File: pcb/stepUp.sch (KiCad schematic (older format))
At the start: 14 parts

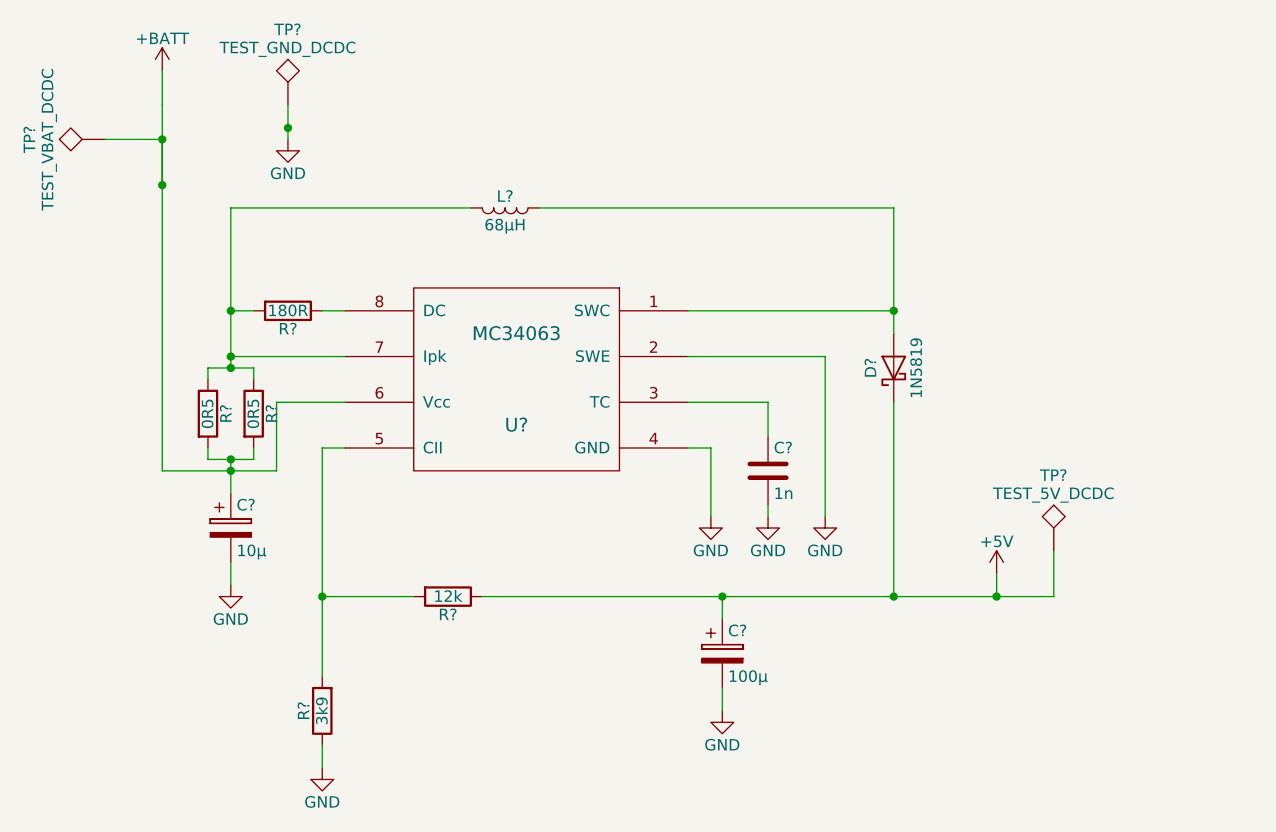
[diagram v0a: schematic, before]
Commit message: nightly | pcb build, routing, placing
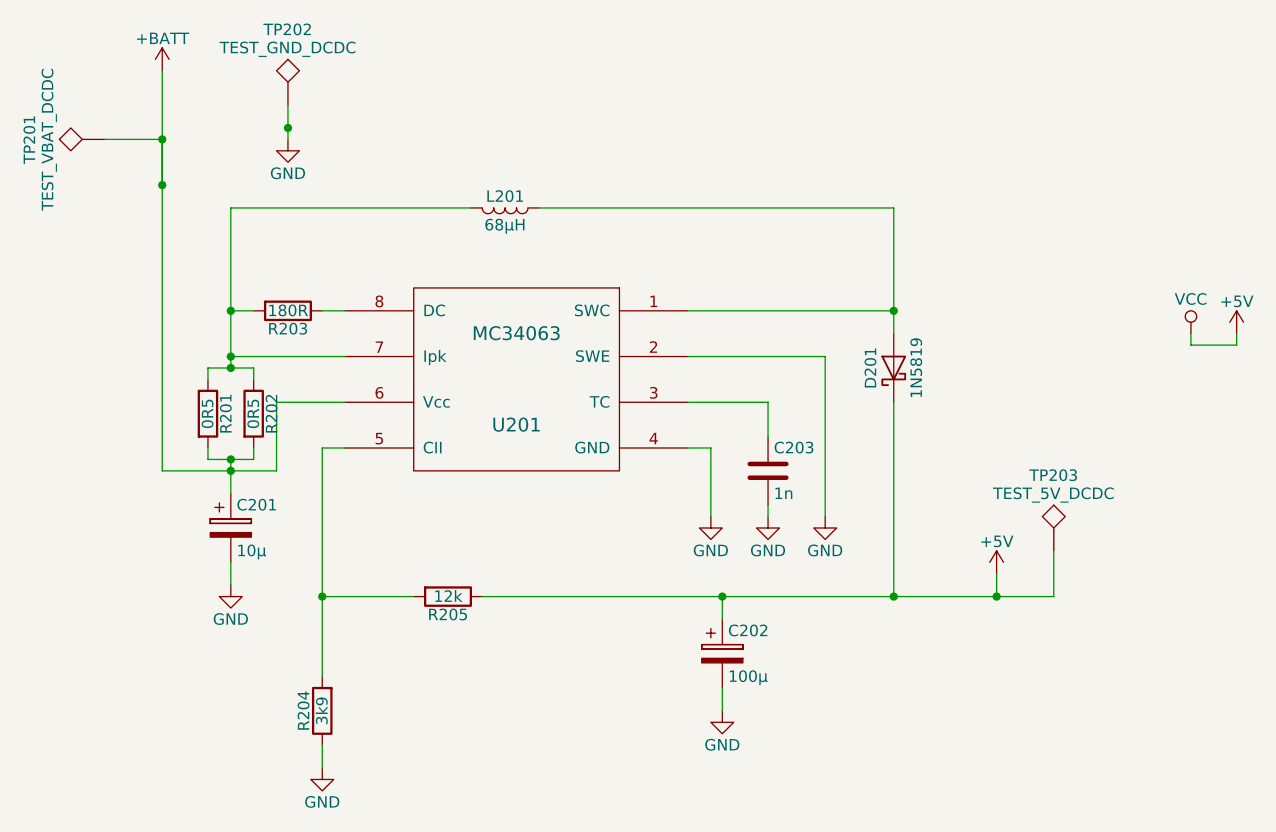
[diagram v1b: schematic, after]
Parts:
- C201, C202: renamed from C?; footprint (none) -> Capacitors_SMD:CP_Elec_10x10.5
- C203: renamed from C?; footprint (none) -> Capacitors_SMD:C_0603_HandSoldering
- D201: renamed from D?; footprint (none) -> Diodes_SMD:D_SMC-RM10_Universal_Handsoldering
- L201: renamed from L?; footprint (none) -> Inductors_SMD:L_Taiyo-Yuden_NR-50xx_HandSoldering
- R201, R202, R203, R204, R205: renamed from R?; footprint (none) -> Resistors_SMD:R_0603_HandSoldering
- TP201, TP202, TP203: renamed from TP?; footprint (none) -> Measurement_Points:Measurement_Point_Round-SMD-Pad_Big
- U201: renamed from U?; footprint (none) -> Housings_SOIC:SOIC-8_3.9x4.9mm_Pitch1.27mm
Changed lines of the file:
@@
 LIBS:contrib
 LIBS:valves
-LIBS:MC34063
 LIBS:adxl345
+LIBS:ws2812b
 LIBS:fantimote-cache
 EELAYER 25 0
@@
 $Descr A4 11693 8268
 encoding utf-8
-Sheet 2 7
+Sheet 2 10
 Title "seniorsRemote (fantimote)"
 Date "2018-07-07"
@@
 $EndDescr
 $Comp
-L MC34063 U?
+L MC34063 U201
 U 1 1 5B367841
 P 2850 2200
-F 0 "U?" H 2850 2000 60  0000 C CNN
+F 0 "U201" H 2850 2000 60  0000 C CNN
 F 1 "MC34063" H 2850 2400 60  0000 C CNN
-F 2 "" H 2850 2200 60  0001 C CNN
+F 2 "Housings_SOIC:SOIC-8_3.9x4.9mm_Pitch1.27mm" H 2850 2200 60  0001 C CNN
 F 3 "" H 2850 2200 60  0001 C CNN
 	1    2850 2200
@@
 $EndComp
 $Comp
-L D_Schottky D?
+L D_Schottky D201
 U 1 1 5B36789E
 P 4500 2150
-F 0 "D?" H 4500 2250 50  0000 C CNN
+F 0 "D201" H 4500 2250 50  0000 C CNN
 F 1 "1N5819" H 4500 2050 50  0000 C CNN
-F 2 "" H 4500 2150 50  0001 C CNN
+F 2 "Diodes_SMD:D_SMC-RM10_Universal_Handsoldering" H 4500 2150 50  0001 C CNN
 F 3 "" H 4500 2150 50  0001 C CNN
 	1    4500 2150
@@
 $EndComp
 $Comp
-L R R?
+L R R204
 U 1 1 5B3678EB
 P 2000 3650
-F 0 "R?" V 2080 3650 50  0000 C CNN
+F 0 "R204" V 2080 3650 50  0000 C CNN
 F 1 "3k9" V 2000 3650 50  0000 C CNN
-F 2 "" V 1930 3650 50  0001 C CNN
+F 2 "Resistors_SMD:R_0603_HandSoldering" V 1930 3650 50  0001 C CNN
 F 3 "" H 2000 3650 50  0001 C CNN
 	1    2000 3650
@@
 $EndComp
 $Comp
-L R R?
+L R R205
 U 1 1 5B367974
 P 2550 3150
-F 0 "R?" V 2630 3150 50  0000 C CNN
+F 0 "R205" V 2630 3150 50  0000 C CNN
 F 1 "12k" V 2550 3150 50  0000 C CNN
-F 2 "" V 2480 3150 50  0001 C CNN
+F 2 "Resistors_SMD:R_0603_HandSoldering" V 2480 3150 50  0001 C CNN
 F 3 "" H 2550 3150 50  0001 C CNN
 	1    2550 3150
@@
 $EndComp
 $Comp
-L R R?
+L R R203
 U 1 1 5B3679D4
 P 1850 1900
-F 0 "R?" V 1930 1900 50  0000 C CNN
+F 0 "R203" V 1930 1900 50  0000 C CNN
 F 1 "180R" V 1850 1900 50  0000 C CNN
-F 2 "" V 1780 1900 50  0001 C CNN
+F 2 "Resistors_SMD:R_0603_HandSoldering" V 1780 1900 50  0001 C CNN
 F 3 "" H 1850 1900 50  0001 C CNN
 	1    1850 1900
@@
 $EndComp
 $Comp
-L CP C?
+L CP C201
 U 1 1 5B367A61
 P 1600 2850
-F 0 "C?" H 1625 2950 50  0000 L CNN
+F 0 "C201" H 1625 2950 50  0000 L CNN
 F 1 "10µ" H 1625 2750 50  0000 L CNN
-F 2 "" H 1638 2700 50  0001 C CNN
+F 2 "Capacitors_SMD:CP_Elec_10x10.5" H 1638 2700 50  0001 C CNN
 F 3 "" H 1600 2850 50  0001 C CNN
 	1    1600 2850
@@
 $EndComp
 $Comp
-L CP C?
+L CP C202
 U 1 1 5B367AE7
 P 3750 3400
-F 0 "C?" H 3775 3500 50  0000 L CNN
+F 0 "C202" H 3775 3500 50  0000 L CNN
 F 1 "100µ" H 3775 3300 50  0000 L CNN
-F 2 "" H 3788 3250 50  0001 C CNN
+F 2 "Capacitors_SMD:CP_Elec_10x10.5" H 3788 3250 50  0001 C CNN
 F 3 "" H 3750 3400 50  0001 C CNN
 	1    3750 3400
@@
 	2100 1900 2000 1900
 $Comp
-L L L?
+L L L201
 U 1 1 5B367BFD
 P 2800 1450
-F 0 "L?" V 2750 1450 50  0000 C CNN
+F 0 "L201" V 2750 1450 50  0000 C CNN
 F 1 "68µH" V 2875 1450 50  0000 C CNN
-F 2 "" H 2800 1450 50  0001 C CNN
+F 2 "Inductors_SMD:L_Taiyo-Yuden_NR-50xx_HandSoldering" H 2800 1450 50  0001 C CNN
 F 3 "" H 2800 1450 50  0001 C CNN
 	1    2800 1450
@@
 $EndComp
 $Comp
-L GND #PWR?
+L GND #PWR03
 U 1 1 5B367CA4
 P 3750 3650
-F 0 "#PWR?" H 3750 3400 50  0001 C CNN
+F 0 "#PWR03" H 3750 3400 50  0001 C CNN
 F 1 "GND" H 3750 3500 50  0000 C CNN
 F 2 "" H 3750 3650 50  0001 C CNN
@@
 $EndComp
 $Comp
-L GND #PWR?
+L GND #PWR04
 U 1 1 5B367CF4
 P 3700 2800
-F 0 "#PWR?" H 3700 2550 50  0001 C CNN
+F 0 "#PWR04" H 3700 2550 50  0001 C CNN
 F 1 "GND" H 3700 2650 50  0000 C CNN
 F 2 "" H 3700 2800 50  0001 C CNN
@@
 $EndComp
 $Comp
-L GND #PWR?
+L GND #PWR05
 U 1 1 5B367D44
 P 2000 3900
-F 0 "#PWR?" H 2000 3650 50  0001 C CNN
+F 0 "#PWR05" H 2000 3650 50  0001 C CNN
 F 1 "GND" H 2000 3750 50  0000 C CNN
 F 2 "" H 2000 3900 50  0001 C CNN
@@
 $EndComp
 $Comp
-L GND #PWR?
+L GND #PWR06
 U 1 1 5B367D6C
 P 1600 3100
-F 0 "#PWR?" H 1600 2850 50  0001 C CNN
+F 0 "#PWR06" H 1600 2850 50  0001 C CNN
 F 1 "GND" H 1600 2950 50  0000 C CNN
 F 2 "" H 1600 3100 50  0001 C CNN
@@
 	1800 2300 1800 2600
 Wire Wire Line
-	1800 2600 1600 2600
-Wire Wire Line
-	1600 2600 1300 2600
+	1800 2600 1300 2600
 Connection ~ 1600 2600
 Wire Wire Line
@@
 	2100 2500 2000 2500
 Wire Wire Line
-	2000 2500 2000 3150
-Wire Wire Line
-	2000 3150 2000 3500
+	2000 2500 2000 3500
 Wire Wire Line
 	2000 3150 2400 3150
@@
 	2000 3800 2000 3900
 Wire Wire Line
-	2700 3150 3750 3150
-Wire Wire Line
-	3750 3150 4500 3150
-Wire Wire Line
-	4500 3150 4950 3150
-Wire Wire Line
-	4950 3150 5200 3150
+	2700 3150 5200 3150
 Wire Wire Line
 	3750 3150 3750 3250
@@
 	4200 2800 4200 2100
 $Comp
-L GND #PWR?
+L GND #PWR07
 U 1 1 5B367D1C
 P 4200 2800
-F 0 "#PWR?" H 4200 2550 50  0001 C CNN
+F 0 "#PWR07" H 4200 2550 50  0001 C CNN
 F 1 "GND" H 4200 2650 50  0000 C CNN
 F 2 "" H 4200 2800 50  0001 C CNN
@@
 	3600 1900 4500 1900
 Wire Wire Line
-	4500 1450 4500 1900
-Wire Wire Line
-	4500 1900 4500 2000
+	4500 1450 4500 2000
 Wire Wire Line
 	4500 3150 4500 2300
@@
 Connection ~ 4500 1900
 $Comp
-L +BATT #PWR?
+L +BATT #PWR08
 U 1 1 5B36829E
 P 1300 850
-F 0 "#PWR?" H 1300 700 50  0001 C CNN
+F 0 "#PWR08" H 1300 700 50  0001 C CNN
 F 1 "+BATT" H 1300 990 50  0000 C CNN
 F 2 "" H 1300 850 50  0001 C CNN
@@
 $EndComp
 $Comp
-L GND #PWR?
+L GND #PWR09
 U 1 1 5B36830C
 P 1850 1150
-F 0 "#PWR?" H 1850 900 50  0001 C CNN
+F 0 "#PWR09" H 1850 900 50  0001 C CNN
 F 1 "GND" H 1850 1000 50  0000 C CNN
 F 2 "" H 1850 1150 50  0001 C CNN
@@
 $EndComp
 Wire Wire Line
-	1300 850  1300 1000
-Wire Wire Line
-	1300 1000 1300 1150
-Wire Wire Line
-	1300 1150 1300 1350
-Wire Wire Line
-	1300 1350 1300 1350
-Wire Wire Line
-	1300 2600 1300 1350
+	1300 2600 1300 850
 Wire Wire Line
 	1300 1350 1300 1150
 Wire Wire Line
-	1850 1100 1850 1150
+	1850 1000 1850 1150
 Connection ~ 1300 1350
 $Comp
-L +5V #PWR?
+L +5V #PWR010
 U 1 1 5B3684BC
 P 4950 3050
-F 0 "#PWR?" H 4950 2900 50  0001 C CNN
+F 0 "#PWR010" H 4950 2900 50  0001 C CNN
 F 1 "+5V" H 4950 3190 50  0000 C CNN
 F 2 "" H 4950 3050 50  0001 C CNN
@@
 Connection ~ 4500 3150
 $Comp
-L TEST TP?
+L TEST TP202
 U 1 1 5B3686AD
 P 1850 1000
-F 0 "TP?" H 1850 1300 50  0000 C BNN
+F 0 "TP202" H 1850 1300 50  0000 C BNN
 F 1 "TEST_GND_DCDC" H 1850 1250 50  0000 C CNN
-F 2 "" H 1850 1000 50  0001 C CNN
+F 2 "Measurement_Points:Measurement_Point_Round-SMD-Pad_Big" H 1850 1000 50  0001 C CNN
 F 3 "" H 1850 1000 50  0001 C CNN
 	1    1850 1000
@@
 $EndComp
 $Comp
-L TEST TP?
+L TEST TP201
 U 1 1 5B3686F8
 P 1050 1150
-F 0 "TP?" H 1050 1450 50  0000 C BNN
+F 0 "TP201" H 1050 1450 50  0000 C BNN
 F 1 "TEST_VBAT_DCDC" H 1050 1400 50  0000 C CNN
-F 2 "" H 1050 1150 50  0001 C CNN
+F 2 "Measurement_Points:Measurement_Point_Round-SMD-Pad_Big" H 1050 1150 50  0001 C CNN
 F 3 "" H 1050 1150 50  0001 C CNN
 	1    1050 1150
@@
 $EndComp
 $Comp
-L TEST TP?
+L TEST TP203
 U 1 1 5B36873C
 P 5200 2950
-F 0 "TP?" H 5200 3250 50  0000 C BNN
+F 0 "TP203" H 5200 3250 50  0000 C BNN
 F 1 "TEST_5V_DCDC" H 5200 3200 50  0000 C CNN
-F 2 "" H 5200 2950 50  0001 C CNN
+F 2 "Measurement_Points:Measurement_Point_Round-SMD-Pad_Big" H 5200 2950 50  0001 C CNN
 F 3 "" H 5200 2950 50  0001 C CNN
 	1    5200 2950
@@
 Connection ~ 4950 3150
 Wire Wire Line
-	1050 1150 1300 1150
+	1300 1150 1050 1150
 Connection ~ 1300 1150
-Wire Wire Line
-	1850 1100 1850 1000
 Connection ~ 1850 1100
 $Comp
-L R R?
+L R R201
 U 1 1 5B3FC151
 P 1500 2350
-F 0 "R?" V 1580 2350 50  0000 C CNN
+F 0 "R201" V 1580 2350 50  0000 C CNN
 F 1 "0R5" V 1500 2350 50  0000 C CNN
-F 2 "" V 1430 2350 50  0001 C CNN
+F 2 "Resistors_SMD:R_0603_HandSoldering" V 1430 2350 50  0001 C CNN
 F 3 "" H 1500 2350 50  0001 C CNN
 	1    1500 2350
@@
 $EndComp
 $Comp
-L R R?
+L R R202
 U 1 1 5B3FC188
 P 1700 2350
-F 0 "R?" V 1780 2350 50  0000 C CNN
+F 0 "R202" V 1780 2350 50  0000 C CNN
 F 1 "0R5" V 1700 2350 50  0000 C CNN
-F 2 "" V 1630 2350 50  0001 C CNN
+F 2 "Resistors_SMD:R_0603_HandSoldering" V 1630 2350 50  0001 C CNN
 F 3 "" H 1700 2350 50  0001 C CNN
 	1    1700 2350
@@
 $EndComp
 Wire Wire Line
-	1600 1450 1600 1900
-Wire Wire Line
-	1600 1900 1600 2100
-Wire Wire Line
-	1600 2100 1600 2150
-Wire Wire Line
-	1600 2550 1600 2600
-Wire Wire Line
-	1600 2600 1600 2700
+	1600 1450 1600 2150
+Wire Wire Line
+	1600 2550 1600 2700
 Wire Wire Line
 	1500 2500 1500 2550
 Wire Wire Line
-	1500 2550 1600 2550
-Wire Wire Line
-	1600 2550 1700 2550
+	1500 2550 1700 2550
 Wire Wire Line
 	1700 2550 1700 2500
@@
 	1500 2200 1500 2150
 Wire Wire Line
-	1500 2150 1600 2150
-Wire Wire Line
-	1600 2150 1700 2150
+	1500 2150 1700 2150
 Wire Wire Line
 	1700 2150 1700 2200
@@
 Connection ~ 1600 2550
 $Comp
-L C C?
+L C C203
 U 1 1 5B3FC69A
 P 3950 2600
-F 0 "C?" H 3975 2700 50  0000 L CNN
+F 0 "C203" H 3975 2700 50  0000 L CNN
 F 1 "1n" H 3975 2500 50  0000 L CNN
-F 2 "" H 3988 2450 50  0001 C CNN
+F 2 "Capacitors_SMD:C_0603_HandSoldering" H 3988 2450 50  0001 C CNN
 F 3 "" H 3950 2600 50  0001 C CNN
 	1    3950 2600
@@
 $EndComp
 $Comp
-L GND #PWR?
+L GND #PWR011
 U 1 1 5B3FC7D4
 P 3950 2800
-F 0 "#PWR?" H 3950 2550 50  0001 C CNN
+F 0 "#PWR011" H 3950 2550 50  0001 C CNN
 F 1 "GND" H 3950 2650 50  0000 C CNN
 F 2 "" H 3950 2800 50  0001 C CNN
@@
 Wire Wire Line
 	3950 2800 3950 2750
+$Comp
+L VCC #PWR012
+U 1 1 5B432150
+P 5800 2000
+F 0 "#PWR012" H 5800 1850 50  0001 C CNN
+F 1 "VCC" H 5800 2150 50  0000 C CNN
+F 2 "" H 5800 2000 50  0001 C CNN
+F 3 "" H 5800 2000 50  0001 C CNN
+	1    5800 2000
+	1    0    0    -1
+$EndComp
+$Comp
+L +5V #PWR013
+U 1 1 5B432180
+P 6000 2000
+F 0 "#PWR013" H 6000 1850 50  0001 C CNN
+F 1 "+5V" H 6000 2140 50  0000 C CNN
+F 2 "" H 6000 2000 50  0001 C CNN
+F 3 "" H 6000 2000 50  0001 C CNN
+	1    6000 2000
+	1    0    0    -1
+$EndComp
+Wire Wire Line
+	6000 2000 6000 2050
+Wire Wire Line
+	6000 2050 5800 2050
+Wire Wire Line
+	5800 2050 5800 2000
 $EndSCHEMATC
